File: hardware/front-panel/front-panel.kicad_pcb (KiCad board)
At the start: 4 copper layers, 180 x 100 mm, 76 parts, among them J1 Conn_02x20_Odd_Even, J10 SMA, J11 SMA, J12 SMA, J13 SMA, J14 SMA, J15 SMA, J16 SMA, J17 SMA, J18 SMA, J19 SMA, J2 Conn_02x20_Odd_Even, J20 SMA, J21 SMA, J22 SMA, J23 SMA, J24 SMA, J25 SMA, J3 Conn_02x20_Odd_Even, J30 OLED 0.96in module on 1x4 soc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, J31 KF128-2.54-10P, J32 KF128-5.0-2P, J33 Qwiic (vertical), J40 Module header 2x6 (shrouded), J411 KF301-5.0-2P, J412 KF301-5.0-2P, Q411 MMBT5551, Q412 MMBT5551, Q421 MMBT5551, Q422 MMBT5551, U401 6N137S-TA1-L, U402 6N137S-TA1-L, U410 SN74AHCT541PWR

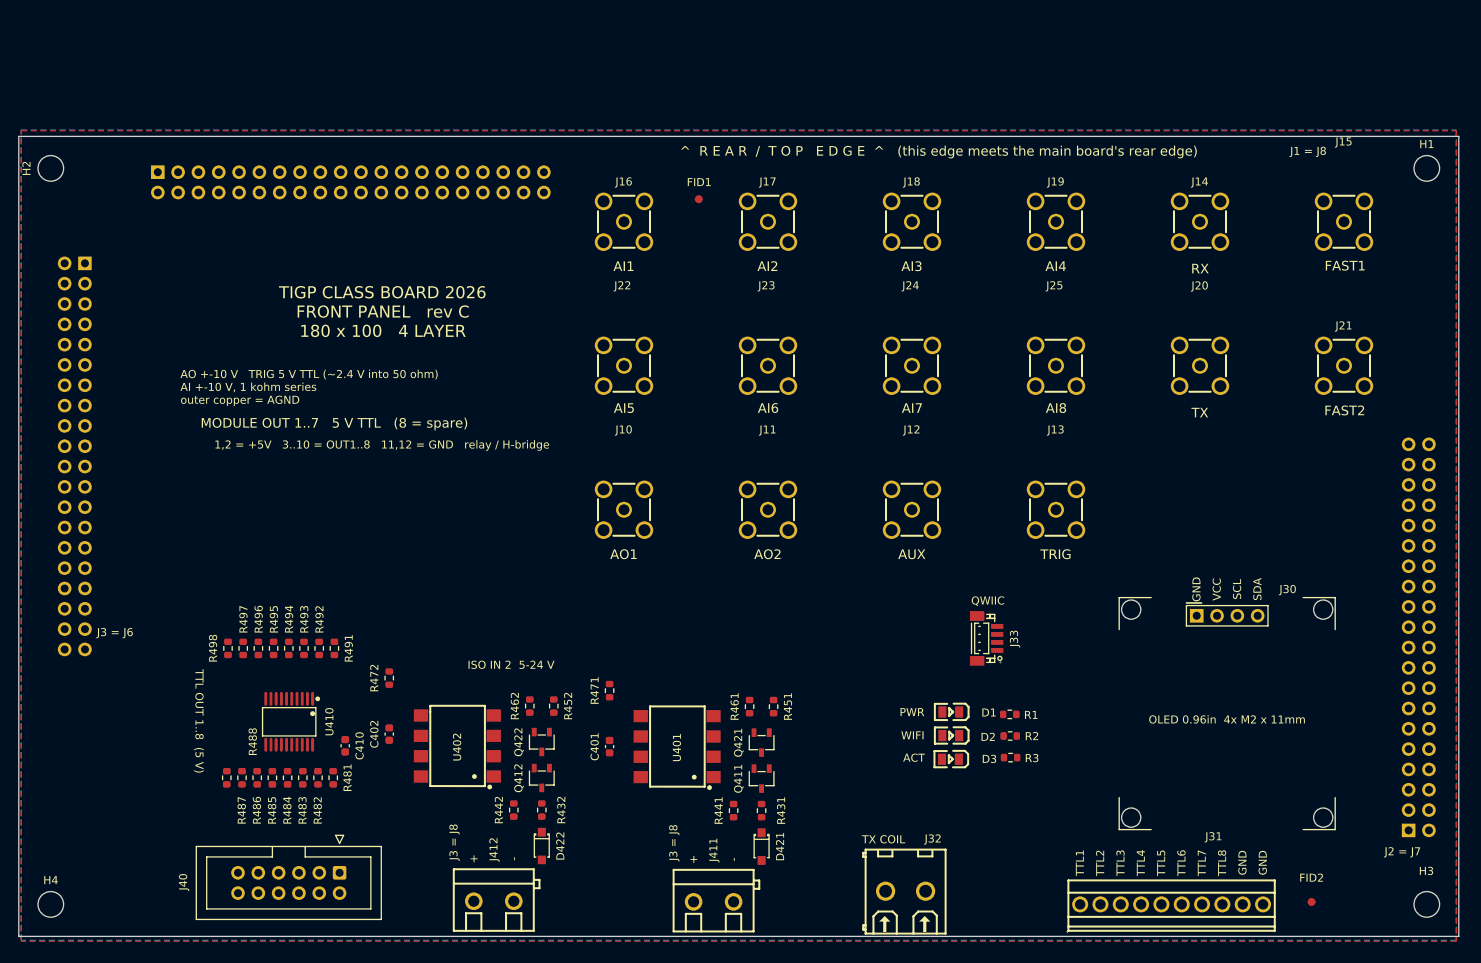
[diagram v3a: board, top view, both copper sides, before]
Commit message: Merge student A (Renqian): area A of the main board (417 tracks/vias, unconnected 197 -> 148) and panel section A (13 analog nets, 121 unconnected left) accepted into the masters; sections re-split
Co-Authored-By: Claude Fable 5.1 <noreply@anthropic.com>
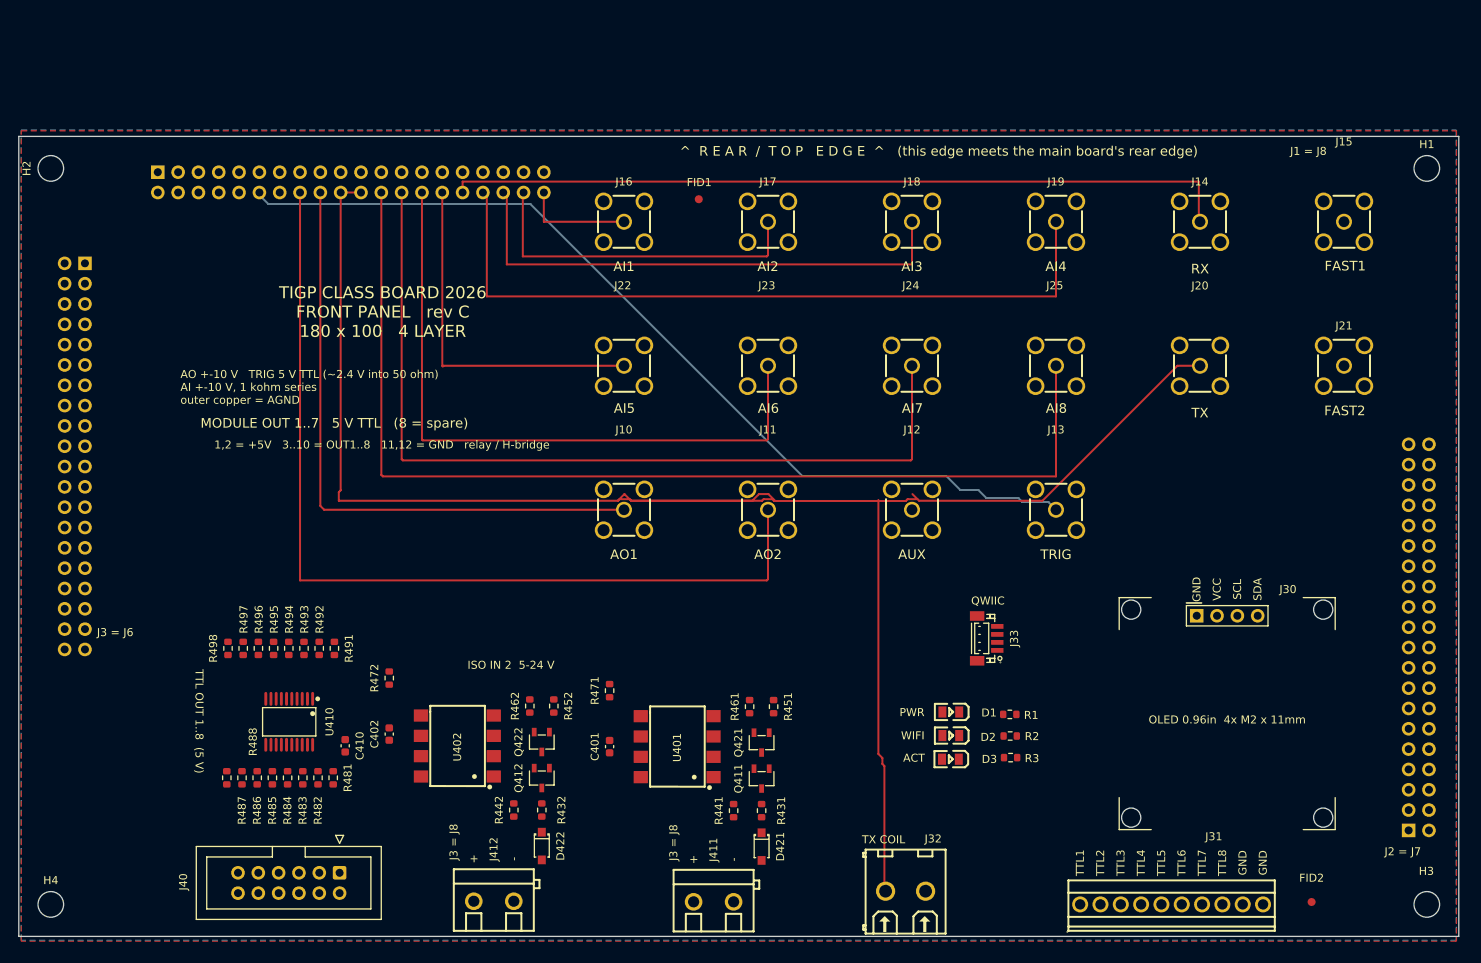
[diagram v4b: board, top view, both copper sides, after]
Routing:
- net /TX: track 0.00 -> 226.3 mm
- net /AI8: track 0.00 -> 133.5 mm
- net /AUX: track 0.00 -> 116.2 mm
- net /AO2: track 0.00 -> 115.7 mm
- net /AI7: track 0.00 -> 108.9 mm
- net /RX: track 0.00 -> 98.5 mm
- net /AI4: track 0.00 -> 94.2 mm
- net /AI6: track 0.00 -> 83.4 mm
- net /AO1: track 0.00 -> 77.3 mm
- net /AI3: track 0.00 -> 65.1 mm
- net /AI5: track 0.00 -> 44.4 mm
- net /AI2: track 0.00 -> 42.9 mm
- net /AI1: track 0.00 -> 13.7 mm

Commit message: WIP masters (instructor), 2026-09-24 14:26
Co-Authored-By: Claude Fable 5.1 <noreply@anthropic.com>
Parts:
- moved J12 18.0 mm to (129.7, 61.7)
- moved J13 18.0 mm to (111.7, 61.7)
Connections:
- J12 pad 1: AGND -> GND
- J12 pad 2: AGND -> GND
- J12 pad 3: AGND -> GND
- J12 pad 4: AGND -> GND
- J14 pad 5: /RX -> /TX
- J15 pad 1: AGND -> GND
- J15 pad 2: AGND -> GND
- J15 pad 3: AGND -> GND
- J15 pad 4: AGND -> GND
- J20 pad 5: /TX -> /RX
- J21 pad 1: AGND -> GND
- J21 pad 2: AGND -> GND
- J21 pad 3: AGND -> GND
- J21 pad 4: AGND -> GND
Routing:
- net /TX: track 226.3 -> 100.3 mm
- net /AUX: track 116.2 -> 82.7 mm
- net /RX: track 98.5 -> 125.1 mm
- net /AI8: track 133.5 -> 108.5 mm
- net /AI7: track 108.9 -> 87.6 mm
- net /AI6: track 83.4 -> 64.9 mm
- net /AI5: track 44.4 -> 33.4 mm
- net /AI4: track 94.2 -> 88.8 mm
- net /AI2: track 42.9 -> 38.3 mm
- net /AI1: track 13.7 -> 11.5 mm
- net /AI3: track 65.1 -> 64.1 mm
- added copper zone on B.Cu, net AGND
- added copper zone on In2.Cu, net AGND
- added copper zone on F.Cu, net GND
- added copper zone on In1.Cu, net GND

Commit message: hardware: panel master with students A/B section routing accepted, from repo main c3a4043
Co-Authored-By: Claude Fable 5.1 <noreply@anthropic.com>
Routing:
- net GND: track 0.00 -> 242.2 mm, vias 0 -> 1
- net /AUX: track 82.7 -> 254.7 mm
- net /TTL1: track 0.00 -> 67.6 mm
- net /TTL2: track 0.00 -> 62.3 mm
- net /TTL3: track 0.00 -> 57.8 mm
- net /TTL4: track 0.00 -> 52.2 mm
- net /TTL5: track 0.00 -> 47.2 mm
- net /TTL6: track 0.00 -> 42.0 mm
- net /TTL7: track 0.00 -> 36.8 mm
- net /FASTTTL1: track 0.00 -> 35.6 mm
- net /TTL8: track 0.00 -> 31.8 mm
- net /FASTTTL2: track 0.00 -> 20.2 mm
- net /LED_ACT_A: track 0.00 -> 5.73 mm
- net /LED_PWR_A: track 0.00 -> 5.62 mm
- net /LED_WIFI_A: track 0.00 -> 5.57 mm

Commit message: hardware: instructor's masters of 2026-09-25 04:25 (main board) and 2026-09-24 22:43 (panel + schematic)
Co-Authored-By: Claude Fable 5.1 <noreply@anthropic.com>
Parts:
- moved R472 8.80 mm to (47.4, 91.5)
- moved C402 6.30 mm to (47.5, 95.9), turned to -90 degrees
- moved R451 5.63 mm to (91.5, 91.1), turned to -90 degrees
- moved R461 5.17 mm to (89.3, 91.0), turned to -90 degrees
- moved R442 4.98 mm to (66.8, 99.3)
- moved R441 4.95 mm to (94.3, 99.2)
- moved R471 4.72 mm to (74.5, 89.0)
- moved Q421 1.70 mm to (94.5, 90.8)
- moved D421 1.36 mm to (92.5, 102.5), turned to 180 degrees
- moved C410 1.33 mm to (39.5, 90.9), turned to 0 degrees
- moved R432 0.98 mm to (64.4, 99.2)
- moved R431 0.75 mm to (92.1, 99.3)
- moved C401 0.72 mm to (73.9, 92.0), turned to 180 degrees
- moved Q411 0.47 mm to (93.3, 95.4), turned to 0 degrees
- turned Q412 to 0 degrees
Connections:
- J14 pad 5: /TX -> /RX
- J20 pad 5: /RX -> /TX
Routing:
- net +3V3: track 0.00 -> 299.0 mm, vias 0 -> 3
- net GND: track 242.2 -> 32.1 mm, vias 1 -> 21
- net /AUX: track 254.7 -> 110.0 mm
- net +5V_RAW: track 0.00 -> 120.2 mm
- net /TX: track 100.3 -> 206.6 mm
- net /OPTO_IN1: track 0.00 -> 89.1 mm
- net /I2C_SDA: track 0.00 -> 65.7 mm
- net /OPTO_IN2: track 0.00 -> 65.5 mm
- net /I2C_SCL: track 0.00 -> 63.8 mm
- net /LED_ACT: track 0.00 -> 56.7 mm
- net /LED_WIFI: track 0.00 -> 56.7 mm
- net /MOD1: track 0.00 -> 51.2 mm
- net /MOD2: track 0.00 -> 46.4 mm
- net /TRIG_5V: track 0.00 -> 45.4 mm
- net /ISO2_IN-: track 0.00 -> 45.3 mm
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- added copper zone on F.Cu, net /TX
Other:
- board text removed: "J1 = J8"
- board text removed: "J1 J2 J3 mate J6 J7 J8 of the main board; pin 1 marked"
- board text removed: "J1 pin 1"
- board text removed: "J1 pin 40"
- board text removed: "J2 pin 1"
- board text removed: "J2 pin 40"

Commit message: hardware: front panel as saved 2026-09-30 22:15
Co-Authored-By: Claude Fable 5.1 <noreply@anthropic.com>
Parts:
- renumbered J20 to J13, J13 to J20
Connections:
- J1 pad 1: AGND -> GND
- J1 pad 10: unconnected-(J1-Pin_10-Pad10) -> /TX
- J1 pad 11: AGND -> GND
- J1 pad 12: /AUX -> /TX
- J1 pad 13: AGND -> unconnected-(J1-Pin_13-Pad13)
- J1 pad 20: /TX -> /AUX
- J1 pad 22: /TX -> /RX
- J1 pad 3: AGND -> GND
- J1 pad 32: /RX -> unconnected-(J1-Pin_32-Pad32)
- J1 pad 5: AGND -> GND
- J1 pad 7: AGND -> GND
- J1 pad 9: AGND -> GND
- J13 pad 5: /TX -> /AUX
- J20 pad 1: AGND -> GND
- J20 pad 2: AGND -> GND
- J20 pad 3: AGND -> GND
- J20 pad 4: AGND -> GND
- J20 pad 5: /AUX -> /TX
- J32 pad 2: AGND -> GND
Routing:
- net /TX: track 206.6 -> 159.8 mm
- net /RX: track 103.6 -> 145.2 mm
- net /AUX: track 110.0 -> 134.5 mm
- net AGND: vias 0 -> 1
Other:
- board text removed: "TX"
